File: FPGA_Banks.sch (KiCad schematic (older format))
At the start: 37 parts

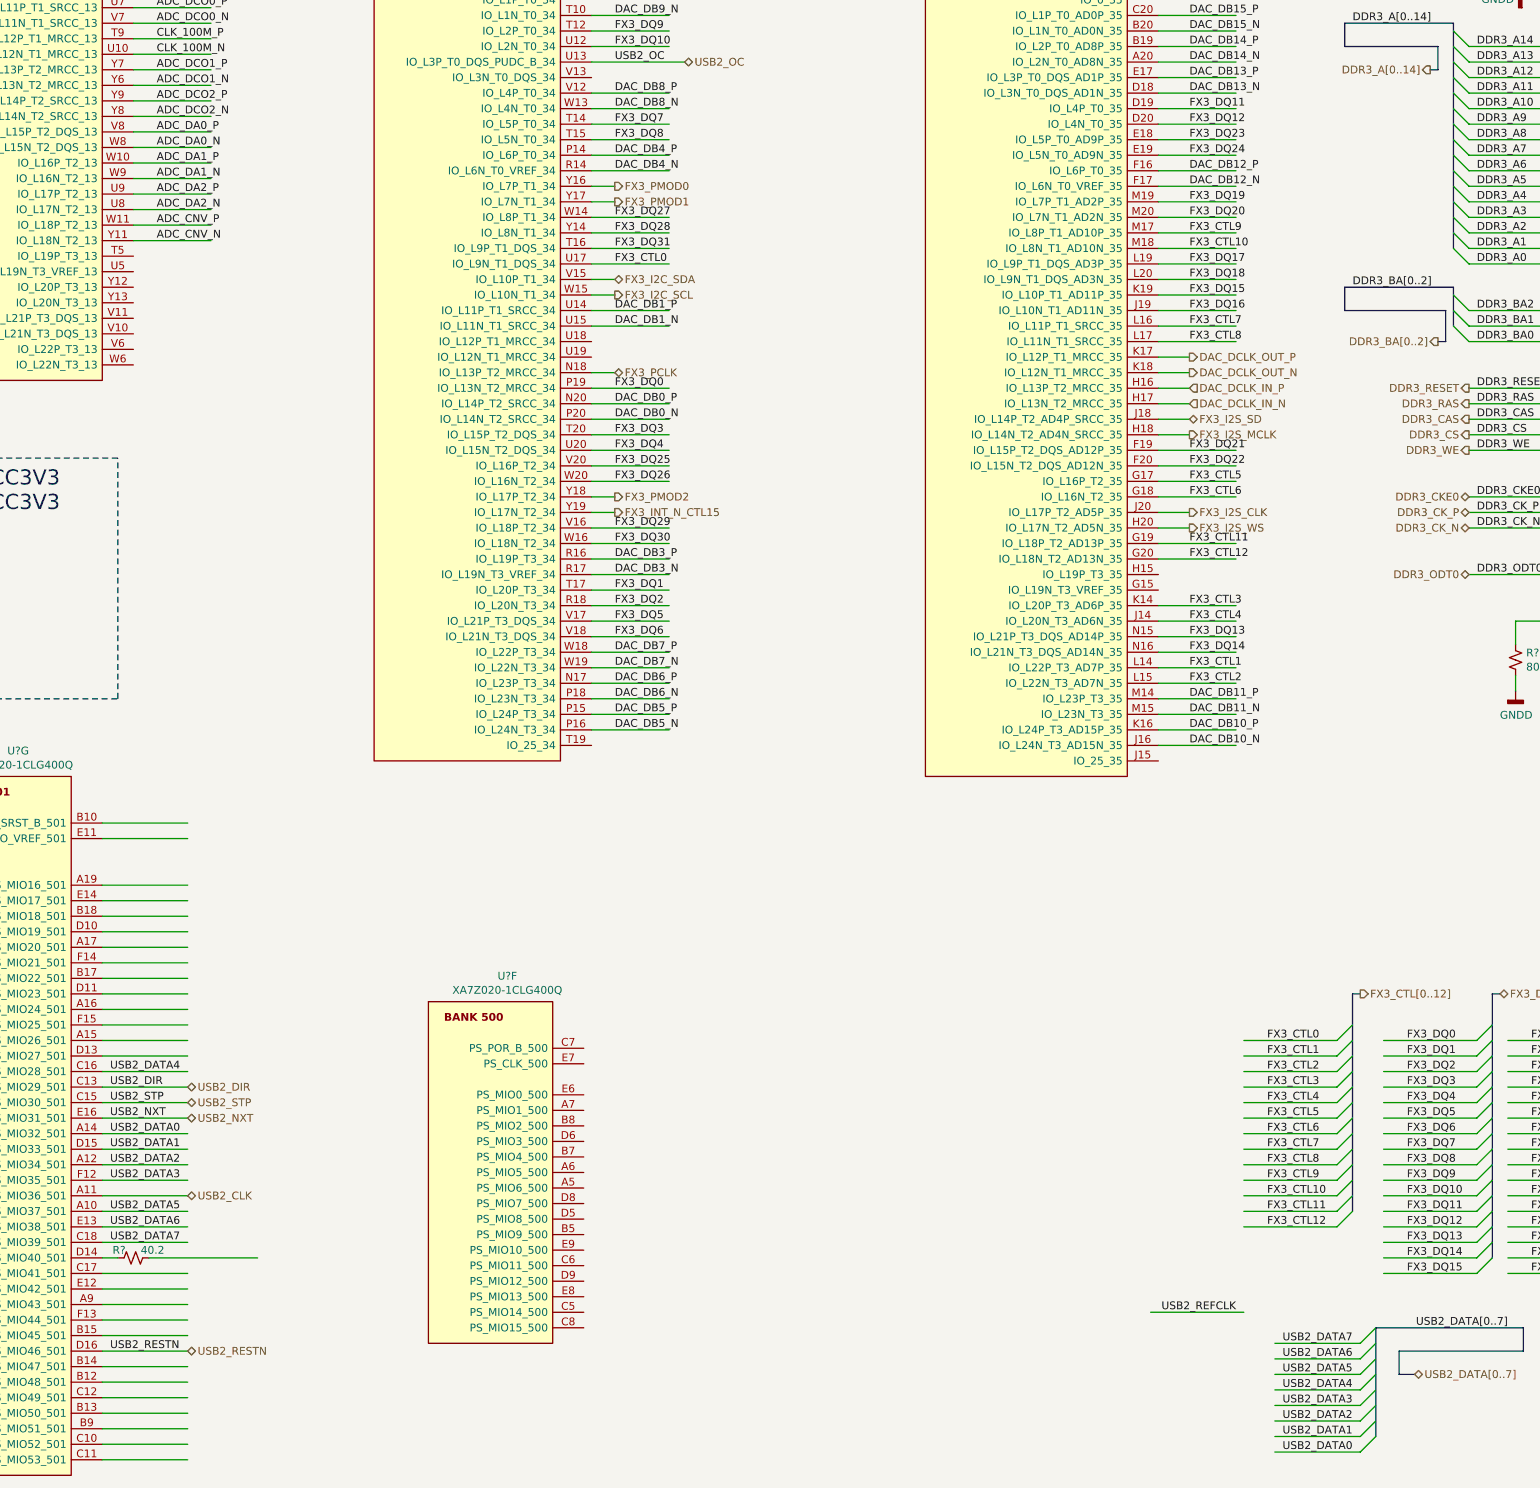
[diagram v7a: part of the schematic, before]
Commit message: Connected Ethernet sheet with FPGA bank
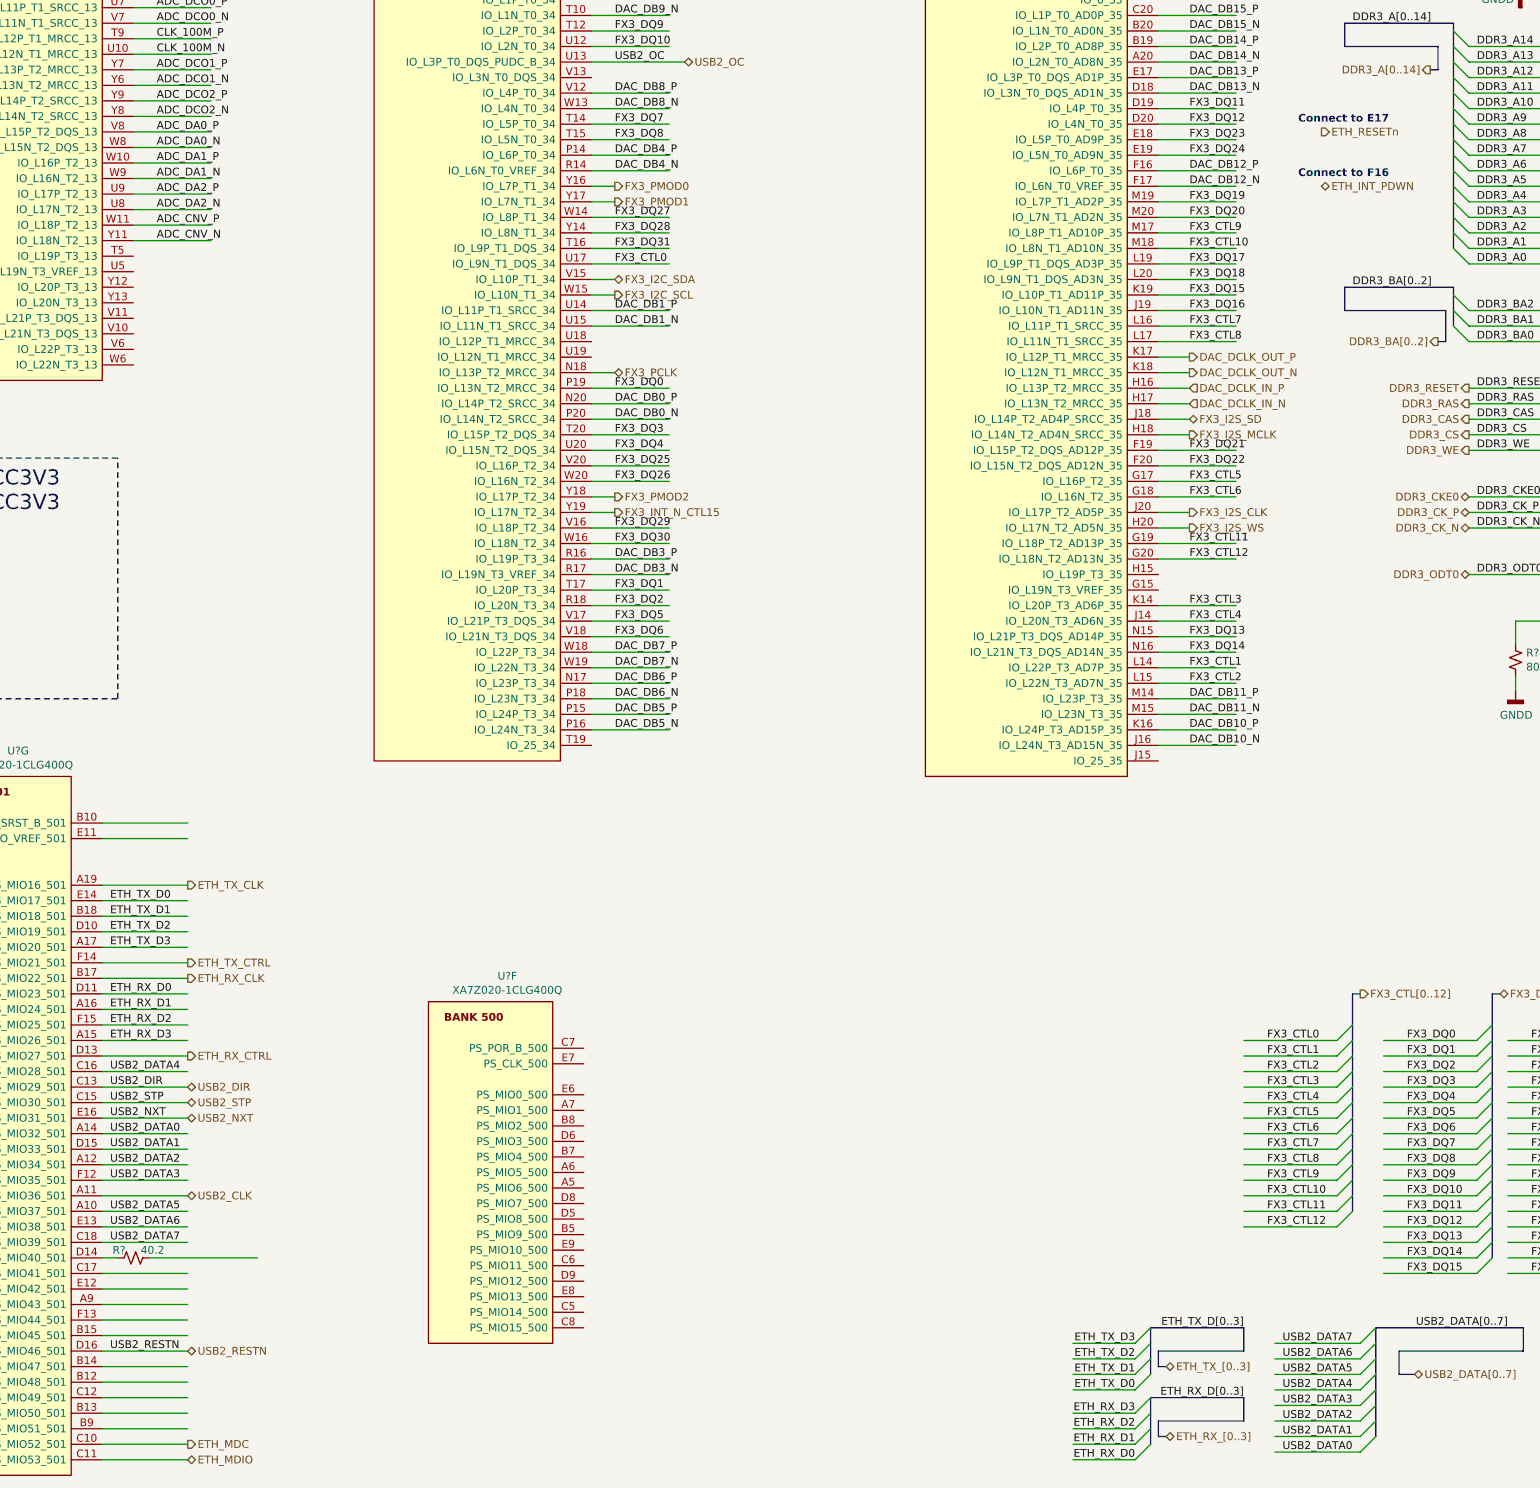
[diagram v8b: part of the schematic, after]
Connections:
- net labels added: ETH_INT_PDWN, ETH_MDC, ETH_MDIO, ETH_RESETn, ETH_RX_CLK, ETH_RX_CTRL, ETH_RX_D0, ETH_RX_D1, ETH_RX_D2, ETH_RX_D3, ETH_RX_D[0..3], ETH_RX_[0..3], ETH_TX_CLK, ETH_TX_CTRL, ETH_TX_D0, ETH_TX_D1, ETH_TX_D2, ETH_TX_D3, ETH_TX_D[0..3], ETH_TX_[0..3]
- net labels removed: USB2_REFCLK
- wire segments 353 -> 360
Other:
- note added: "Connect to E17\n"
- note added: "Connect to F16\n"
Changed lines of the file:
@@
 $Descr A3 16535 11693
 encoding utf-8
-Sheet 24 25
+Sheet 23 25
 Title ""
 Date ""
@@
 Text Label 10550 10850 2    50   ~ 0
 USB2_DATA0
-Text Label 9800 9950 2    50   ~ 0
-USB2_REFCLK
 Entry Wire Line
 	10700 10750 10600 10850
@@
 Text Label 11550 10050 2    50   ~ 0
 USB2_DATA[0..7]
-Wire Wire Line
-	9250 9950 9850 9950
 Wire Wire Line
 	10600 10150 10050 10150
@@
 Wire Wire Line
 	2700 1850 3200 1850
-Wire Bus Line
-	11200 3350 11200 3600
-Wire Bus Line
-	10700 10050 10700 10750
-Wire Bus Line
-	11200 1650 11200 3100
-Wire Bus Line
-	15150 8100 15150 9600
-Wire Bus Line
-	13300 8100 13300 9600
-Wire Bus Line
-	10550 7900 10550 9300
-Wire Bus Line
-	11450 7900 11450 9600
-Wire Bus Line
-	12250 7900 12250 9600
 Text Notes 1500 950  0    50   ~ 0
 Set Bank13 to 2.5V. ADC need 2.5V signaling
+Text HLabel 3050 7200 2    50   Output ~ 0
+ETH_TX_CLK
+Text HLabel 3050 7700 2    50   Output ~ 0
+ETH_TX_CTRL
+Text Label 9150 10450 2    50   ~ 0
+ETH_TX_D0
+Text Label 9150 10350 2    50   ~ 0
+ETH_TX_D1
+Text Label 9150 10250 2    50   ~ 0
+ETH_TX_D2
+Text Label 9150 10150 2    50   ~ 0
+ETH_TX_D3
+Entry Wire Line
+	9250 10050 9150 10150
+Entry Wire Line
+	9250 10150 9150 10250
+Entry Wire Line
+	9250 10250 9150 10350
+Entry Wire Line
+	9250 10350 9150 10450
+Text HLabel 9350 10300 2    50   BiDi ~ 0
+ETH_TX_[0..3]
+Text Label 9850 10050 2    50   ~ 0
+ETH_TX_D[0..3]
+Wire Wire Line
+	8750 10450 9150 10450
+Wire Wire Line
+	8750 10350 9150 10350
+Wire Wire Line
+	8750 10250 9150 10250
+Wire Wire Line
+	8750 10150 9150 10150
+Wire Bus Line
+	9350 10300 9300 10300
+Wire Bus Line
+	9300 10300 9300 10200
+Wire Bus Line
+	9300 10200 9850 10200
+Wire Bus Line
+	9850 10200 9850 10050
+Wire Bus Line
+	9850 10050 9250 10050
+Text HLabel 3050 7800 2    50   Output ~ 0
+ETH_RX_CLK
+Text HLabel 3050 8300 2    50   Output ~ 0
+ETH_RX_CTRL
+Text Label 9150 10900 2    50   ~ 0
+ETH_RX_D0
+Text Label 9150 10800 2    50   ~ 0
+ETH_RX_D1
+Text Label 9150 10700 2    50   ~ 0
+ETH_RX_D2
+Text Label 9150 10600 2    50   ~ 0
+ETH_RX_D3
+Entry Wire Line
+	9250 10500 9150 10600
+Entry Wire Line
+	9250 10600 9150 10700
+Entry Wire Line
+	9250 10700 9150 10800
+Entry Wire Line
+	9250 10800 9150 10900
+Text HLabel 9350 10750 2    50   BiDi ~ 0
+ETH_RX_[0..3]
+Text Label 9850 10500 2    50   ~ 0
+ETH_RX_D[0..3]
+Wire Wire Line
+	8750 10900 9150 10900
+Wire Wire Line
+	8750 10800 9150 10800
+Wire Wire Line
+	8750 10700 9150 10700
+Wire Wire Line
+	8750 10600 9150 10600
+Wire Bus Line
+	9850 10650 9300 10650
+Wire Bus Line
+	9300 10650 9300 10750
+Wire Bus Line
+	9300 10750 9350 10750
+Wire Bus Line
+	9850 10500 9250 10500
+Text HLabel 3050 10900 2    50   BiDi ~ 0
+ETH_MDIO
+Text HLabel 3050 10800 2    50   Output ~ 0
+ETH_MDC
+Wire Bus Line
+	9850 10500 9850 10650
+Text HLabel 10350 2700 2    50   BiDi ~ 0
+ETH_INT_PDWN
+Text HLabel 10350 2350 2    50   Output ~ 0
+ETH_RESETn
+Text Label 2550 7300 0    50   ~ 0
+ETH_TX_D0
+Text Label 2550 7400 0    50   ~ 0
+ETH_TX_D1
+Text Label 2550 7500 0    50   ~ 0
+ETH_TX_D2
+Text Label 2550 7600 0    50   ~ 0
+ETH_TX_D3
+Text Label 2550 7900 0    50   ~ 0
+ETH_RX_D0
+Text Label 2550 8000 0    50   ~ 0
+ETH_RX_D1
+Text Label 2550 8100 0    50   ~ 0
+ETH_RX_D2
+Text Label 2550 8200 0    50   ~ 0
+ETH_RX_D3
+Text Notes 10200 2650 0    50   ~ 10
+Connect to F16\n
+Text Notes 10200 2300 0    50   ~ 10
+Connect to E17\n
+Wire Bus Line
+	11200 3350 11200 3600
+Wire Bus Line
+	9250 10050 9250 10350
+Wire Bus Line
+	9250 10500 9250 10800
+Wire Bus Line
+	10700 10050 10700 10750
+Wire Bus Line
+	11200 1650 11200 3100
+Wire Bus Line
+	15150 8100 15150 9600
+Wire Bus Line
+	13300 8100 13300 9600
+Wire Bus Line
+	10550 7900 10550 9300
+Wire Bus Line
+	11450 7900 11450 9600
+Wire Bus Line
+	12250 7900 12250 9600
 $EndSCHEMATC
